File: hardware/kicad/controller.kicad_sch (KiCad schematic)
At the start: 9 parts, among them J1 Debug UART, SW1 RESET, U1 Raspberry Pi Pico 2

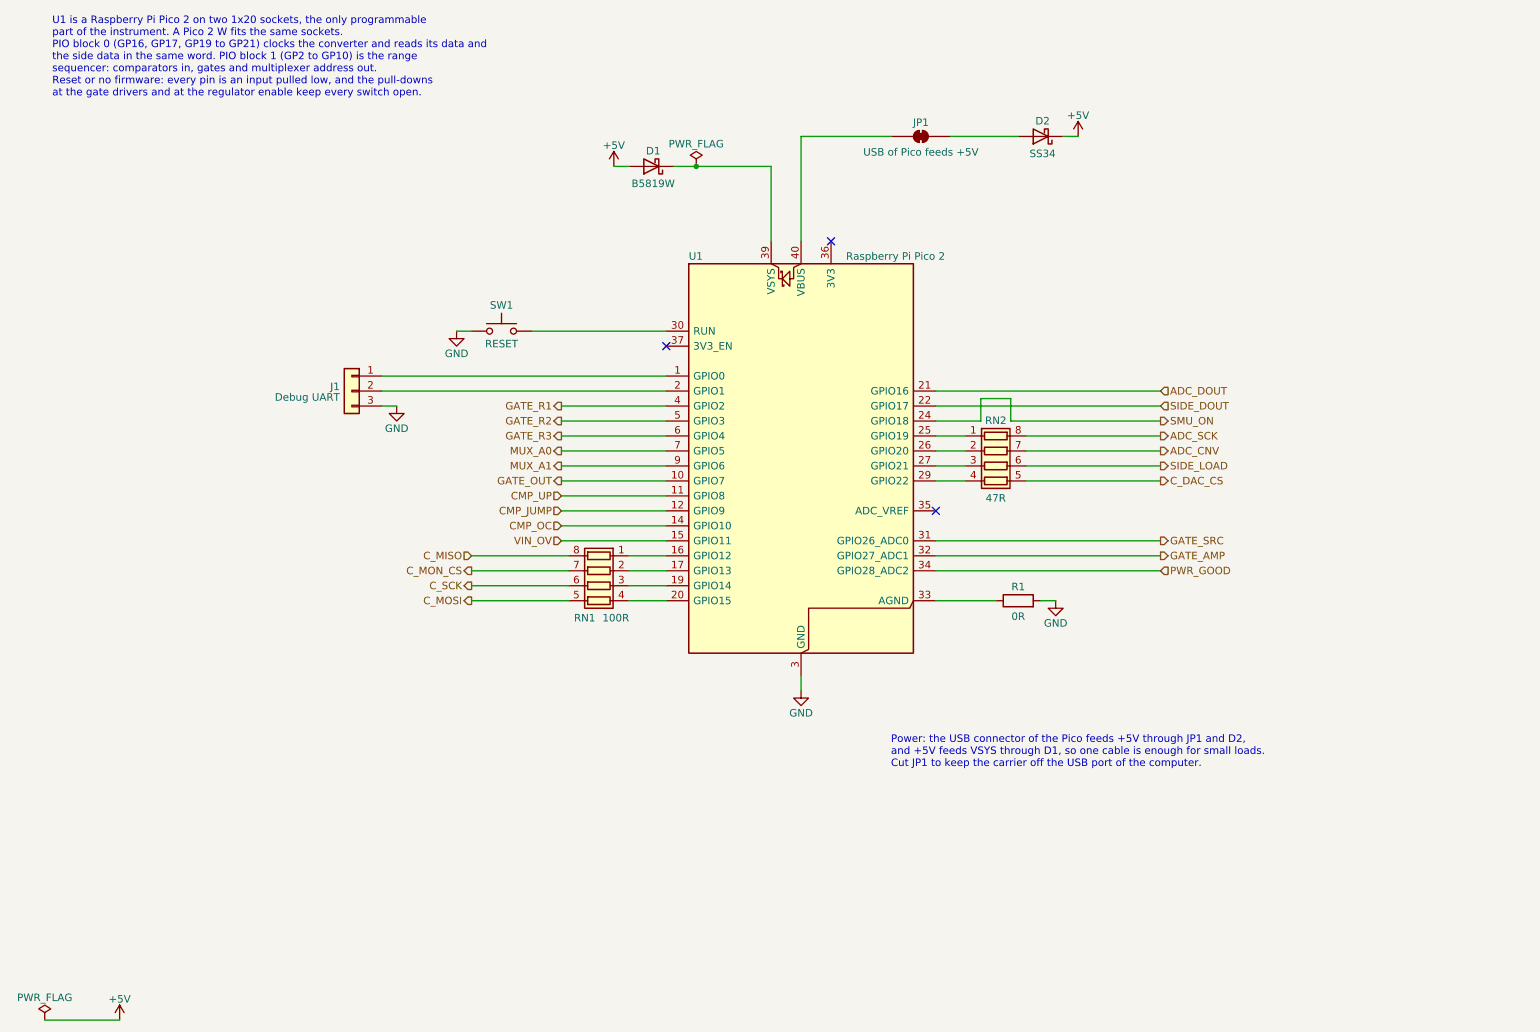
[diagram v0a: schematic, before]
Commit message: feat(hardware): draw draft A2 of the schematic
428 parts on 15 A4 pages, 14 sheets below the root sheet (D-83). Two
sheets are new: Logic Supplies, with the supervisor of the 5 V rail and
the two 3.3 V regulators, and Rail Monitor, with the comparators behind
PWR_GOOD.

The drawings follow the specification of draft A2: a current limiter
on each supply input and a priority multiplexer, a pre-regulator that
tracks the output of the linear regulator, a VIN path that withstands
-20 V to +20 V with its switch open, two diode-connected MOSFETs as
ladder clamp, thin-film and four-terminal shunts, ESD arrays at the CC
pins and at the VCC pin of the logic port. The reference designators
are numbered as KiCad numbers them (D-45), so they are not those of
draft A1.

The project library gains the symbol of the input multiplexer and two
footprints: the lever terminal block with pads of 1.9 mm x 2.3 mm and
the controller module without its antenna keep-out (D-85).

The electrical rules check reports no errors and no warnings. The
parts are candidates, and nothing is built or measured.
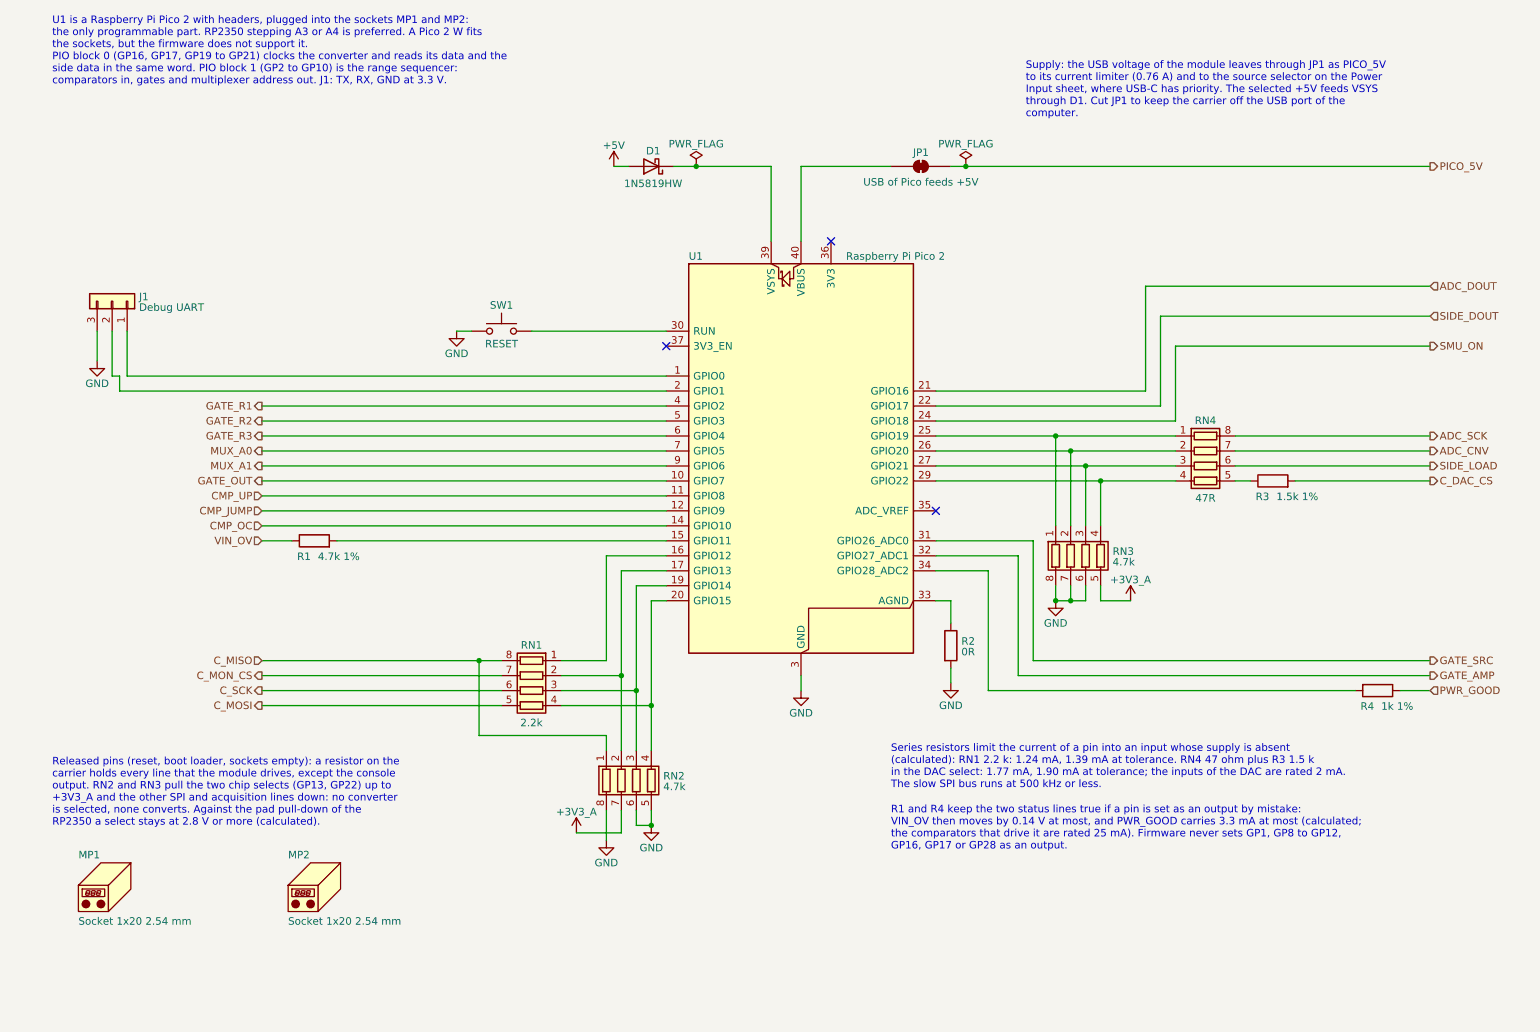
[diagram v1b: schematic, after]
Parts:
- removed D2: SS34, Diode_SMD:D_SMA, symbol Device:D_Schottky
- added MP1, MP2: Socket 1x20 2.54 mm, symbol Mechanical:Housing
- added R1: 4.7k 1%, Resistor_SMD:R_0603_1608Metric, symbol Device:R
- added R3: 1.5k 1%, Resistor_SMD:R_0603_1608Metric, symbol Device:R
- added R4: 1k 1%, Resistor_SMD:R_0603_1608Metric, symbol Device:R
- added RN2, RN3: 4.7k, Resistor_SMD:R_Array_Convex_4x0603, symbol Device:R_Pack04
- D1: value B5819W -> 1N5819HW; MPN (none) -> 1N5819HW-7-F; Manufacturer (none) -> Diodes Incorporated
- J1: MPN (none) -> 61300311121; Manufacturer (none) -> Wurth Elektronik
- JP1: now left out of the parts list
- R2: renamed from R1; MPN (none) -> CRCW06030000Z0EA; Manufacturer (none) -> Vishay
- RN1: value 100R -> 2.2k; MPN (none) -> CAY16-222J4LF; Manufacturer (none) -> Bourns
- RN4: renamed from RN2; MPN (none) -> CAY16-470J4LF; Manufacturer (none) -> Bourns
- SW1: MPN (none) -> B3F-1000; Manufacturer (none) -> Omron
- U1: footprint Module:RaspberryPi_Pico_Common_THT -> PowerProfiler:RaspberryPi_Pico_Common_THT_NoKeepout; MPN (none) -> SC1632; Manufacturer (none) -> Raspberry Pi; Note On two 1x20 pin sockets, 2.54 mm; a Pico 2 W fits the same 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 -> With headers; plugged into two 1x20 pin sockets, not solder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
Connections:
- net C_DAC_CS: now also R3.2; no longer RN4.5 (R4.2)
- net C_MISO: now also RN2.1 (R1.1)
- net GND: now also RN2.5 (R4.2), RN2.6 (R3.2), RN2.8 (R1.2), RN3.6 (R3.2), RN3.7 (R2.2), RN3.8 (R1.2)
- net PWR_GOOD: now also R4.1; no longer U1.34 (GPIO28_ADC2)
- net VIN_OV: now also R1.1; no longer U1.15 (GPIO11)
- net PICO_5V: now reaches JP1.2 (B)
- net at RN1.2 (R2.1), U1.17 (GPIO13): now also RN2.2 (R2.1)
- net at RN1.3 (R3.1), U1.19 (GPIO14): now also RN2.3 (R3.1)
- net at RN1.4 (R4.1), U1.20 (GPIO15): now also RN2.4 (R4.1)
- net at RN4.1 (R1.1), U1.25 (GPIO19): now also RN3.1 (R1.1)
- net at RN4.2 (R2.1), U1.26 (GPIO20): now also RN3.2 (R2.1)
- net at RN4.3 (R3.1), U1.27 (GPIO21): now also RN3.3 (R3.1)
- net at RN4.4 (R4.1), U1.29 (GPIO22): now also RN3.4 (R4.1)
- new net: R1.2, U1.15 (GPIO11)
- new net: R4.2, U1.34 (GPIO28_ADC2)
- new net: R3.1, RN4.5 (R4.2)
- new net +3V3_A: RN2.7 (R2.2), RN3.5 (R4.2)
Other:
- note added: "R1 and R4 keep the two status lines true if a pin is set as an output by mistake: VIN_OV then moves by 0.14 V at most, and PWR_GOOD carries 3.3 mA at most (calculated; the comparators that drive it are rated 25 mA). Firmware never sets GP1, GP8 to GP12, GP16, GP17 or GP28 as an output."
- note added: "Released pins (reset, boot loader, sockets empty): a resistor on the carrier holds every line that the module drives, except the console output. RN2 and RN3 pull the two chip selects (GP13, GP22) up to +3V3_A and the other SPI and acquisition lines down: no converter is selected, none converts. Against the pad pull-down of the RP2350 a select stays at 2.8 V or more (calculated)."
- note added: "Series resistors limit the current of a pin into an input whose supply is absent (calculated): RN1 2.2 k: 1.24 mA, 1.39 mA at tolerance. RN4 47 ohm plus R3 1.5 k in the DAC select: 1.77 mA, 1.90 mA at tolerance; the inputs of the DAC are rated 2 mA. The slow SPI bus runs at 500 kHz or less."
- note added: "Supply: the USB voltage of the module leaves through JP1 as PICO_5V to its current limiter (0.76 A) and to the source selector on the Power Input sheet, where USB-C has priority. The selected +5V feeds VSYS through D1. Cut JP1 to keep the carrier off the USB port of the computer."
- note added: "U1 is a Raspberry Pi Pico 2 with headers, plugged into the sockets MP1 and MP2: the only programmable part. RP2350 stepping A3 or A4 is preferred. A Pico 2 W fits the sockets, but the firmware does not support it. PIO block 0 (GP16, GP17, GP19 to GP21) clocks the converter and reads its data and the side data in the same word. PIO block 1 (GP2 to GP10) is the range sequencer: comparators in, gate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"
- note removed: "Power: the USB connector of the Pico feeds +5V through JP1 and D2, and +5V feeds VSYS through D1, so one cable is enough for small loads. Cut JP1 to keep the carrier off the USB port of the computer."
- note removed: "U1 is a Raspberry Pi Pico 2 on two 1x20 sockets, the only programmable part of the instrument. A Pico 2 W fits the same sockets. PIO block 0 (GP16, GP17, GP19 to GP21) clocks the converter and reads its data and the side data in the same word. PIO block 1 (GP2 to GP10) is the range sequencer: comparators in, gates and multiplexer address out. Reset or no firmware: every pin is an input pulled low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"
- moved on the sheet: J1, JP1, R2, RN1, RN4
